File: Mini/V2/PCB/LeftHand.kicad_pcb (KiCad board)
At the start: 2 copper layers, 155.9 x 99.3 mm, 30 parts

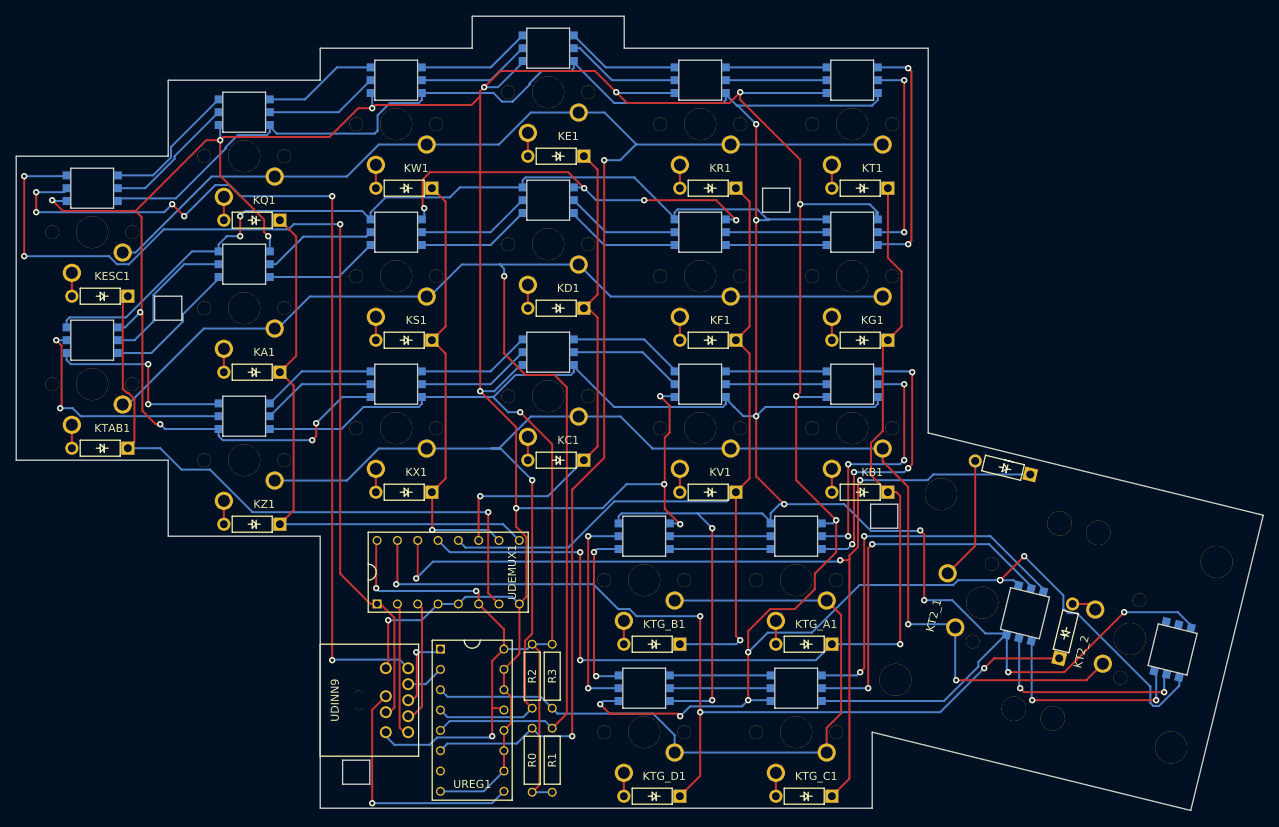
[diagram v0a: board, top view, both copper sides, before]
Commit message: Fixing wiring from peg hole increase.  Regenerating gerber files for left hand.
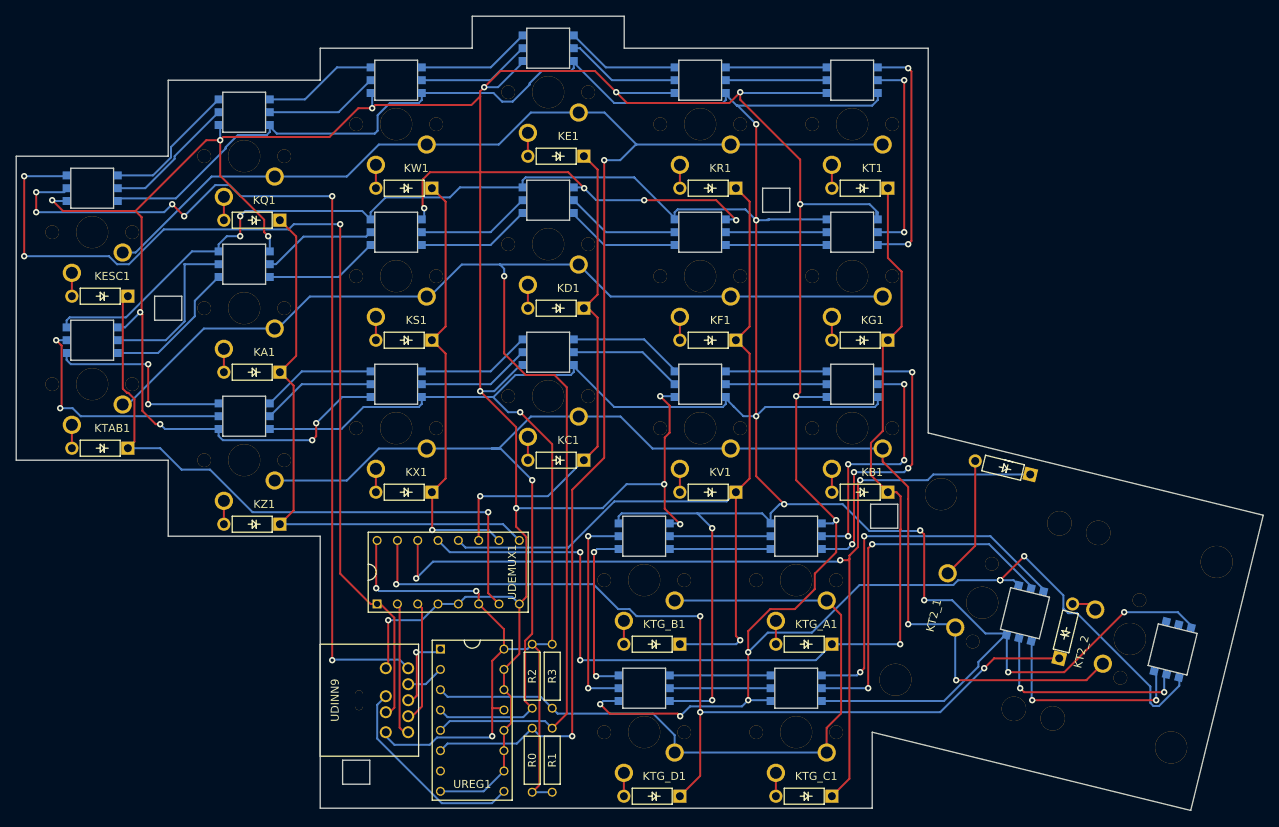
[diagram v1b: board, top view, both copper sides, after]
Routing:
- net RX: track 31.2 -> 25.6 mm, vias 1 -> 0
- net Net-(KA1-Pad6): track 18.9 -> 21.2 mm
- net VCC: track 635.1 -> 633.7 mm
